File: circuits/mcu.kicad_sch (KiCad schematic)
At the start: 36 parts, among them J1 USB_MINI_B, J2 USB_MINI_B, J7 C192300, Q5 Q_L8050QLT1G, Q6 Q_L8550HQLT1G, SW1 SW_PUSH, SW2 SW_PUSH, SW3 SW_PUSH, U10 CP2102N-Axx-xQFN28, U9 ESP32-S3-WROOM-1

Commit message: Resolve USB connector source match
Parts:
- J1, J2: LCSC C46391 -> C5120592; Part Number 920-462A2021S10101 -> 65100516121
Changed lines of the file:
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@@
       (effects (font (size 1.27 1.27)) hide)
     )
-    (property "Part Number" "920-462A2021S10101" (at 129.8956 185.1914 0)
+    (property "Part Number" "65100516121" (at 129.8956 185.1914 0)
       (effects (font (size 1.27 1.27)) hide)
     )
@@
       (effects (font (size 1.27 1.27)) hide)
     )
-    (property "LCSC" "C46391" (at 132.4356 208.0514 0)
+    (property "LCSC" "C5120592" (at 132.4356 208.0514 0)
       (effects (font (size 1.27 1.27)) hide)
     )
@@
       (effects (font (size 1.27 1.27)) hide)
     )
-    (property "Part Number" "920-462A2021S10101" (at 131.9276 144.5514 0)
+    (property "Part Number" "65100516121" (at 131.9276 144.5514 0)
       (effects (font (size 1.27 1.27)) hide)
     )
@@
       (effects (font (size 1.27 1.27)) hide)
     )
-    (property "LCSC" "C46391" (at 134.4676 167.4114 0)
-      (effects (font (size 1.27 1.27)) hide)
-    )
+    (property "LCSC" "C5120592" (at 134.4676 167.4114 0)
+      (effects (font (size 1.27 1.27)) hide)
+    )

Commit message: Checkpoint laser controller fab parity package
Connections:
- net CP2102_VBUS: now reaches C45.1, R55.1, R56.2, U10.8 (VBUS)
- net USB_NATIVE_CONN_VBUS: now reaches D13.2 (A), J2.1 (VBUS)
- net CP2102_RST: now reaches R57.2, U10.9 (~{RST})
- net CP2102_SUSPEND_N: now reaches R58.1, U10.11 (~{SUSPEND})
- net AUTO_EN_BASE: now reaches Q5.1 (B), R50.2
- net USB_UART_CONN_VBUS: now reaches D10.2 (A), J1.1 (VBUS)
- net AUTO_BOOT_BASE: now reaches Q6.1 (B), R51.2

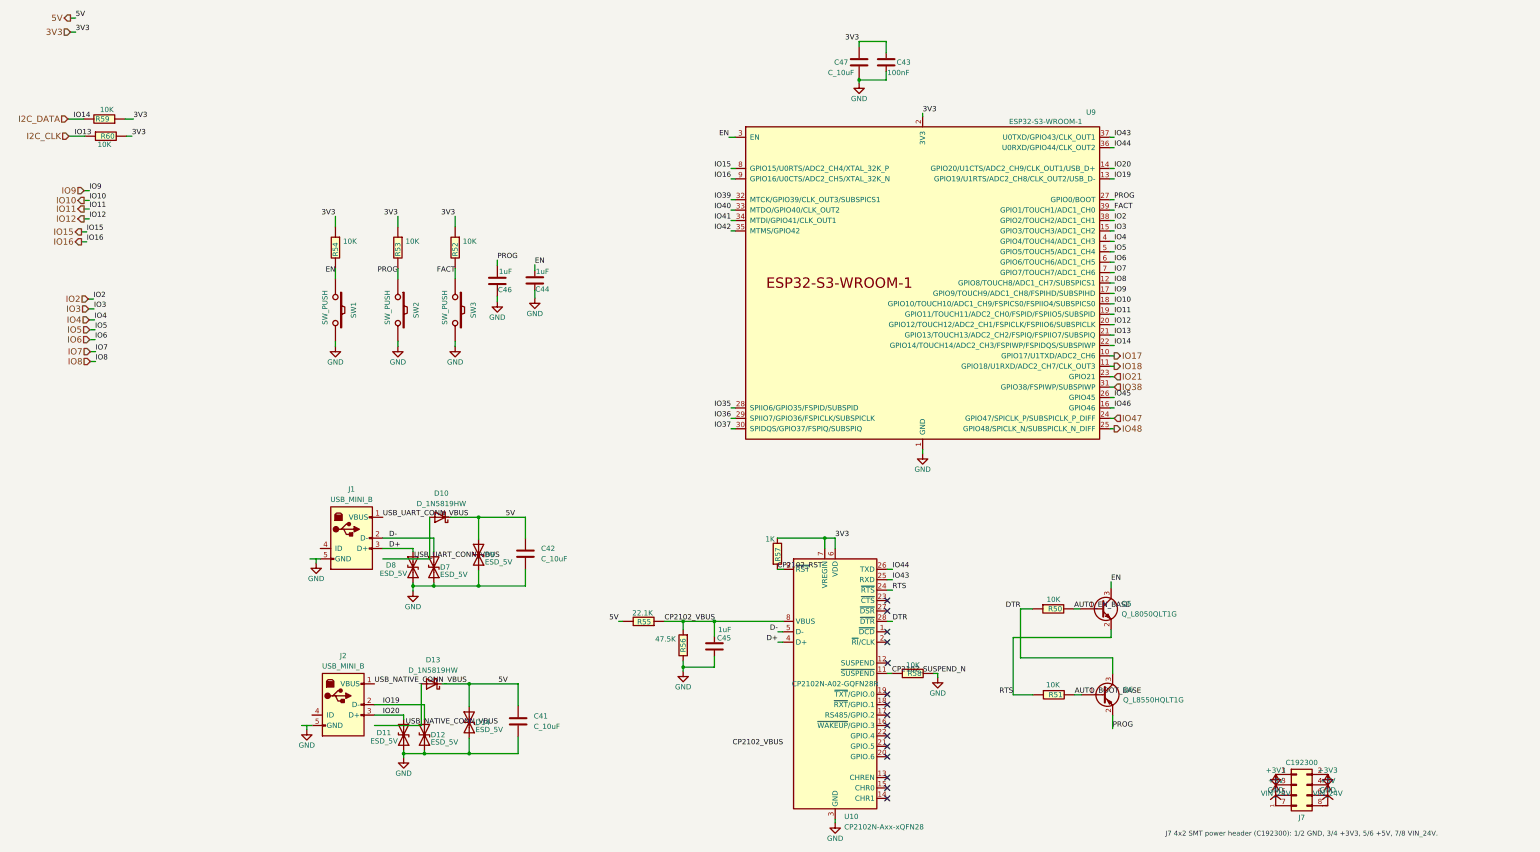
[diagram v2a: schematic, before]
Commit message: Checkpoint schematic ERC errors
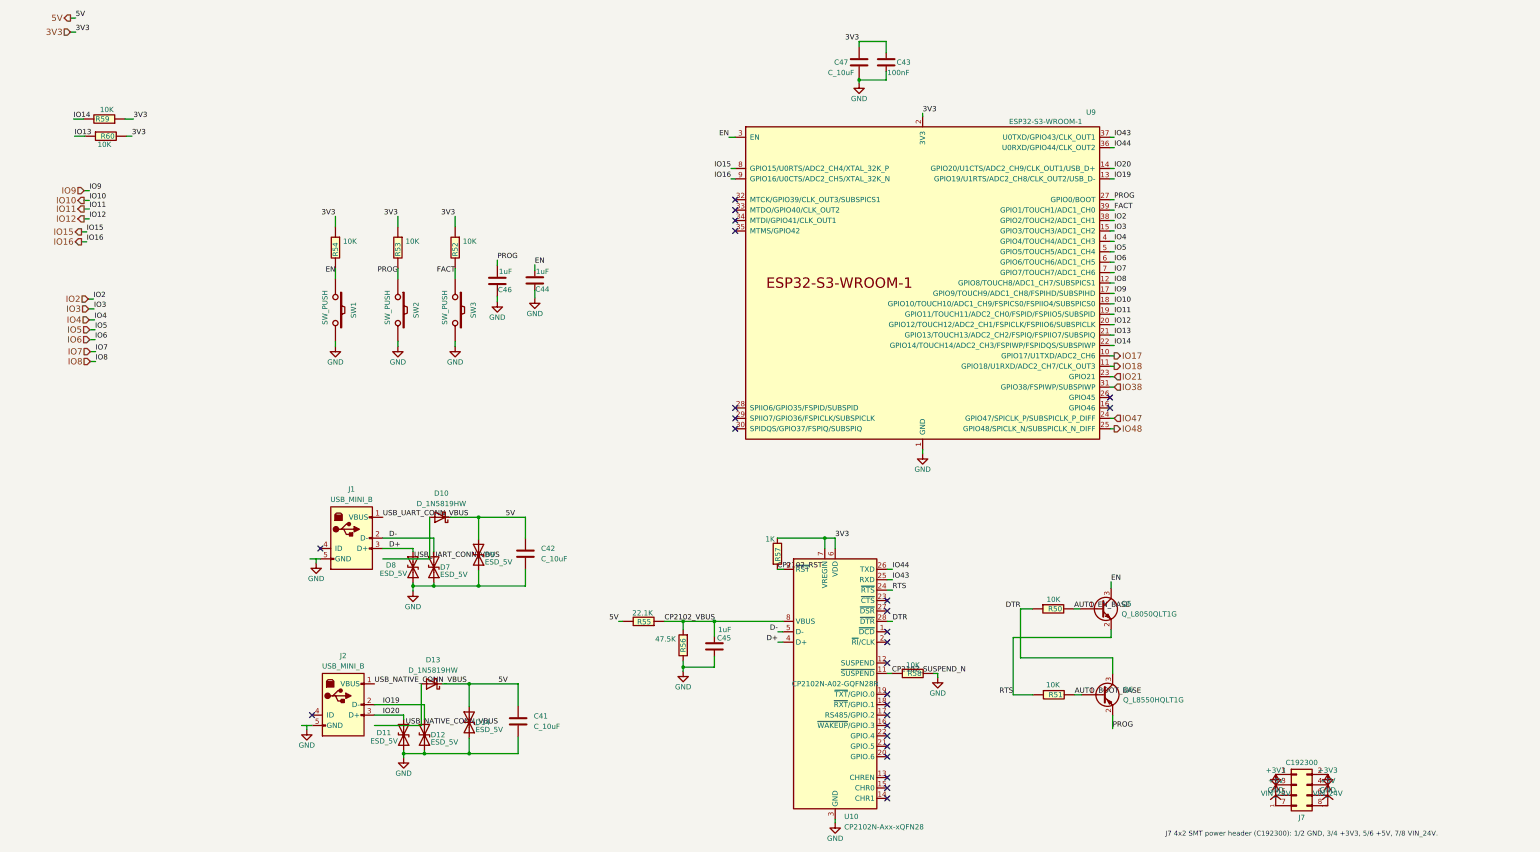
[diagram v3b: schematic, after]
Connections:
- net I2C_CLK renamed IO13
- net I2C_DATA renamed IO14
- net IO35: no longer names the net of U9.28 (SPIIO6/GPIO35/FSPID/SUBSPID)
- net IO36: no longer names the net of U9.29 (SPIIO7/GPIO36/FSPICLK/SUBSPICLK)
- net IO37: no longer names the net of U9.30 (SPIDQS/GPIO37/FSPIQ/SUBSPIQ)
- net IO39: no longer names the net of U9.32 (MTCK/GPIO39/CLK_OUT3/SUBSPICS1)
- net IO40: no longer names the net of U9.33 (MTDO/GPIO40/CLK_OUT2)
- net IO41: no longer names the net of U9.34 (MTDI/GPIO41/CLK_OUT1)
- net IO42: no longer names the net of U9.35 (MTMS/GPIO42)
- net IO45: no longer names the net of U9.26 (GPIO45)
- net IO46: no longer names the net of U9.16 (GPIO46)
- no-connect marks 15 -> 26
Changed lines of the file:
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@@
   (no_connect (at 265.1506 211.8614))
   (no_connect (at 265.1506 209.3214))
-  (no_connect (at 265.2776 189.0014))
+  (no_connect (at 265.1506 189.0014))
   (no_connect (at 265.1506 183.9214))
   (no_connect (at 265.1506 204.2414))
   (no_connect (at 265.1506 199.1614))
   (no_connect (at 265.1506 176.3014))
+  (no_connect (at 126.8476 161.0614))
+  (no_connect (at 124.8156 201.7014))
+  (no_connect (at 228.0666 75.9714))
+  (no_connect (at 228.0666 78.5114))
+  (no_connect (at 228.0666 81.0514))
+  (no_connect (at 228.0666 83.5914))
+  (no_connect (at 228.0666 126.7714))
+  (no_connect (at 228.0666 129.3114))
+  (no_connect (at 228.0666 131.8514))
+  (no_connect (at 319.5066 124.2314))
+  (no_connect (at 319.5066 126.7714))
   (wire (pts (xy 142.0876 163.6014) (xy 153.5176 163.6014))
     (stroke (width 0) (type default))
@@
     (stroke (width 0) (type default))
   )
-  (wire (pts (xy 320.5226 124.2314) (xy 319.5066 124.2314))
-    (stroke (width 0) (type default))
-  )
   (wire (pts (xy 147.1676 211.0994) (xy 147.1676 212.1154))
     (stroke (width 0) (type default))
@@
     (stroke (width 0) (type default))
   )
-  (wire (pts (xy 227.0506 78.5114) (xy 228.0666 78.5114))
-    (stroke (width 0) (type default))
-  )
   (wire (pts (xy 147.1676 210.3374) (xy 147.1676 211.0994))
     (stroke (width 0) (type default))
@@
     (stroke (width 0) (type default))
   )
-  (wire (pts (xy 227.0506 81.0514) (xy 228.0666 81.0514))
-    (stroke (width 0) (type default))
-  )
   (wire (pts (xy 215.3666 178.8414) (xy 215.3666 180.8734))
     (stroke (width 0) (type default))
@@
     (stroke (width 0) (type default))
   )
-  (wire (pts (xy 227.0506 126.7714) (xy 228.0666 126.7714))
-    (stroke (width 0) (type default))
-  )
   (wire (pts (xy 320.5226 75.9714) (xy 319.5066 75.9714))
     (stroke (width 0) (type default))
@@
     (stroke (width 0) (type default))
   )
-  (wire (pts (xy 65.5066 60.4774) (xy 69.4436 60.4774))
+  (wire (pts (xy 66.9036 60.4774) (xy 69.4436 60.4774))
     (stroke (width 0) (type default))
   )
@@
     (stroke (width 0) (type default))
   )
-  (wire (pts (xy 227.0506 75.9714) (xy 228.0666 75.9714))
-    (stroke (width 0) (type default))
-  )
   (wire (pts (xy 147.1676 201.7014) (xy 140.0556 201.7014))
     (stroke (width 0) (type default))
@@
     (stroke (width 0) (type default))
   )
-  (wire (pts (xy 227.0506 83.5914) (xy 228.0666 83.5914))
-    (stroke (width 0) (type default))
-  )
-  (wire (pts (xy 227.0506 129.3114) (xy 228.0666 129.3114))
-    (stroke (width 0) (type default))
-  )
-  (wire (pts (xy 320.5226 126.7714) (xy 319.5066 126.7714))
-    (stroke (width 0) (type default))
-  )
   (wire (pts (xy 227.0506 70.8914) (xy 228.0666 70.8914))
     (stroke (width 0) (type default))
@@
     (stroke (width 0) (type default))
   )
-  (wire (pts (xy 65.2526 56.2864) (xy 69.0626 56.2864))
+  (wire (pts (xy 66.6496 56.2864) (xy 69.0626 56.2864))
     (stroke (width 0) (type default))
   )
@@
     (stroke (width 0) (type default))
   )
-  (wire (pts (xy 227.0506 131.8514) (xy 228.0666 131.8514))
-    (stroke (width 0) (type default))
-  )
   (wire (pts (xy 149.4536 170.2054) (xy 149.4536 171.4754))
     (stroke (width 0) (type default))
@@
     (effects (font (size 1.27 1.27)) (justify right bottom))
   )
-  (label "IO39" (at 227.0506 75.9714 180) (fields_autoplaced)
-    (effects (font (size 1.27 1.27)) (justify right bottom))
-  )
   (label "IO11" (at 320.5226 103.9114 0) (fields_autoplaced)
     (effects (font (size 1.27 1.27)) (justify left bottom))
@@
     (effects (font (size 1.27 1.27)) (justify right bottom))
   )
-  (label "IO41" (at 227.0506 81.0514 180) (fields_autoplaced)
-    (effects (font (size 1.27 1.27)) (justify right bottom))
-  )
   (label "IO43" (at 266.4206 168.6814 0) (fields_autoplaced)
     (effects (font (size 1.27 1.27)) (justify left bottom))
@@
     (effects (font (size 1.27 1.27)) (justify left bottom))
   )
-  (label "IO37" (at 227.0506 131.8514 180) (fields_autoplaced)
-    (effects (font (size 1.27 1.27)) (justify right bottom))
-  )
-  (label "IO42" (at 227.0506 83.5914 180) (fields_autoplaced)
-    (effects (font (size 1.27 1.27)) (justify right bottom))
-  )
   (label "PROG" (at 145.7706 94.0054 180) (fields_autoplaced)
     (effects (font (size 1.27 1.27)) (justify right bottom))
@@
     (effects (font (size 1.27 1.27)) (justify left bottom))
   )
-  (label "IO40" (at 227.0506 78.5114 180) (fields_autoplaced)
-    (effects (font (size 1.27 1.27)) (justify right bottom))
-  )
   (label "IO13" (at 66.9036 60.4774 0) (fields_autoplaced)
     (effects (font (size 1.27 1.27)) (justify left bottom))
   )
-  (label "IO45" (at 320.5226 124.2314 0) (fields_autoplaced)
-    (effects (font (size 1.27 1.27)) (justify left bottom))
-  )
   (label "IO10" (at 320.5226 101.3714 0) (fields_autoplaced)
     (effects (font (size 1.27 1.27)) (justify left bottom))
@@
     (effects (font (size 1.27 1.27)) (justify left bottom))
   )
-  (label "IO35" (at 227.0506 126.7714 180) (fields_autoplaced)
-    (effects (font (size 1.27 1.27)) (justify right bottom))
-  )
   (label "IO3" (at 71.628 102.616 0) (fields_autoplaced)
     (effects (font (size 1.27 1.27)) (justify left bottom))
@@
     (effects (font (size 1.27 1.27)) (justify left bottom))
   )
-  (label "IO46" (at 320.5226 126.7714 0) (fields_autoplaced)
-    (effects (font (size 1.27 1.27)) (justify left bottom))
-  )
   (label "D-" (at 143.6116 158.5214 0) (fields_autoplaced)
     (effects (font (size 1.27 1.27)) (justify left bottom))
   )
-  (label "IO36" (at 227.0506 129.3114 180) (fields_autoplaced)
-    (effects (font (size 1.27 1.27)) (justify right bottom))
-  )
   (label "IO5" (at 320.5226 88.6714 0) (fields_autoplaced)
     (effects (font (size 1.27 1.27)) (justify left bottom))
@@
   (label "CP2102_VBUS" (at 210.7946 178.8414 0)
     (effects (font (size 1.27 1.27)) (justify left bottom))
-  )
-  (label "CP2102_VBUS" (at 239.7506 209.3214 180)
-    (effects (font (size 1.27 1.27)) (justify right bottom))
   )
   (label "CP2102_RST" (at 238.3536 166.1414 0)
@@
     (effects (font (size 1.524 1.524)) (justify right))
   )
-  (hierarchical_label "I2C_DATA" (shape input) (at 65.2526 56.2864 180) (fields_autoplaced)
-    (effects (font (size 1.524 1.524)) (justify right))
-  )
   (hierarchical_label "IO6" (shape input) (at 70.612 110.109 180) (fields_autoplaced)
     (effects (font (size 1.524 1.524)) (justify right))
@@
     (effects (font (size 1.524 1.524)) (justify right))
   )
-  (hierarchical_label "I2C_CLK" (shape input) (at 65.5066 60.4774 180) (fields_autoplaced)
-    (effects (font (size 1.524 1.524)) (justify right))
-  )

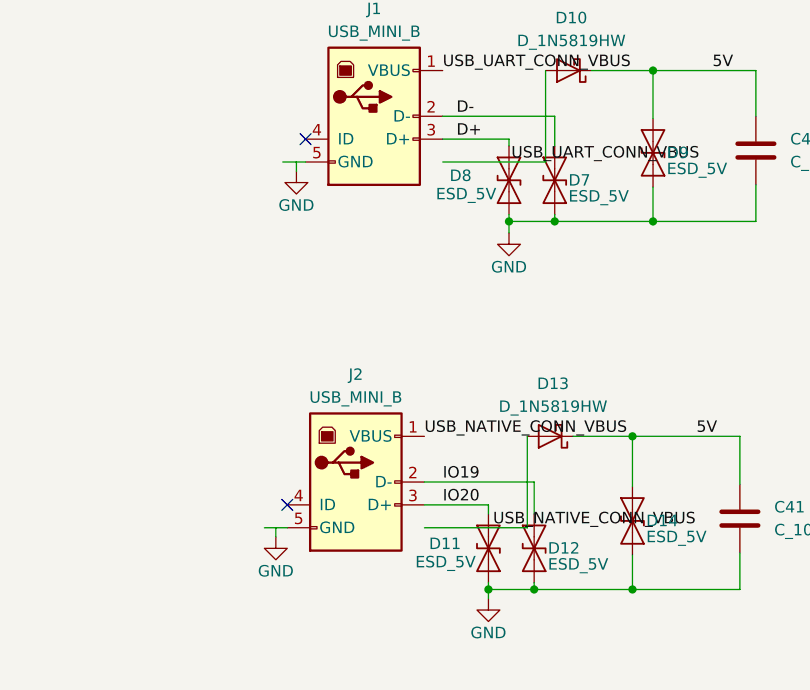
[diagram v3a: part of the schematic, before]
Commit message: Checkpoint schematic warning hygiene
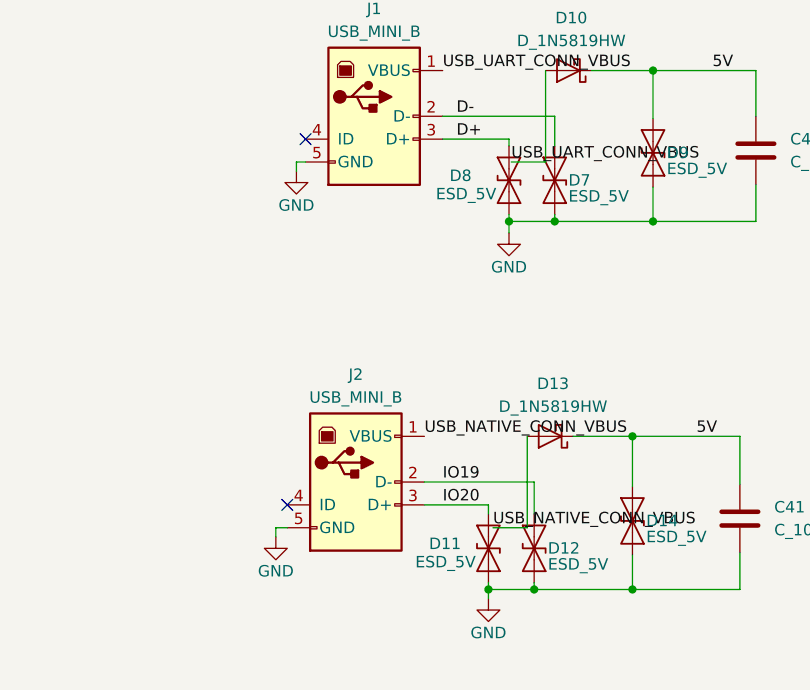
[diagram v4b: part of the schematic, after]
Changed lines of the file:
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@@
   (no_connect (at 319.5066 124.2314))
   (no_connect (at 319.5066 126.7714))
-  (wire (pts (xy 142.0876 163.6014) (xy 153.5176 163.6014))
+  (wire (pts (xy 149.7076 163.6014) (xy 153.5176 163.6014))
     (stroke (width 0) (type default))
   )
@@
     (stroke (width 0) (type default))
   )
-  (wire (pts (xy 124.3076 163.6014) (xy 125.8316 163.6014))
-    (stroke (width 0) (type default))
-  )
   (wire (pts (xy 69.215 80.645) (xy 70.485 80.645))
     (stroke (width 0) (type default))
@@
     (stroke (width 0) (type default))
   )
-  (wire (pts (xy 140.0556 204.2414) (xy 151.4856 204.2414))
+  (wire (pts (xy 147.6756 204.2414) (xy 151.4856 204.2414))
     (stroke (width 0) (type default))
   )
@@
     (stroke (width 0) (type default))
   )
-  (wire (pts (xy 122.2756 204.2414) (xy 123.5456 204.2414))
-    (stroke (width 0) (type default))
-  )

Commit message: Prepare laser controller JLCPCB connector assembly package
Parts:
- J1, J2: LCSC C5120592 -> C46391; Part Number 65100516121 -> 920-462A2021S10101
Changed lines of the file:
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@@
       (effects (font (size 1.27 1.27)) hide)
     )
-    (property "Part Number" "65100516121" (at 129.8956 185.1914 0)
+    (property "Part Number" "920-462A2021S10101" (at 129.8956 185.1914 0)
       (effects (font (size 1.27 1.27)) hide)
     )
@@
       (effects (font (size 1.27 1.27)) hide)
     )
-    (property "LCSC" "C5120592" (at 132.4356 208.0514 0)
+    (property "LCSC" "C46391" (at 132.4356 208.0514 0)
       (effects (font (size 1.27 1.27)) hide)
     )
@@
       (effects (font (size 1.27 1.27)) hide)
     )
-    (property "Part Number" "65100516121" (at 131.9276 144.5514 0)
+    (property "Part Number" "920-462A2021S10101" (at 131.9276 144.5514 0)
       (effects (font (size 1.27 1.27)) hide)
     )
@@
       (effects (font (size 1.27 1.27)) hide)
     )
-    (property "LCSC" "C5120592" (at 134.4676 167.4114 0)
-      (effects (font (size 1.27 1.27)) hide)
-    )
+    (property "LCSC" "C46391" (at 134.4676 167.4114 0)
+      (effects (font (size 1.27 1.27)) hide)
+    )

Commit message: Fix JLCPCB connector assembly package
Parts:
- J1, J2: LCSC C46391 -> C53207143; Part Number 920-462A2021S10101 -> MINI-USB-5P
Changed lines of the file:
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@@
       (effects (font (size 1.27 1.27)) hide)
     )
-    (property "Part Number" "920-462A2021S10101" (at 129.8956 185.1914 0)
+    (property "Part Number" "MINI-USB-5P" (at 129.8956 185.1914 0)
       (effects (font (size 1.27 1.27)) hide)
     )
@@
       (effects (font (size 1.27 1.27)) hide)
     )
-    (property "LCSC" "C46391" (at 132.4356 208.0514 0)
+    (property "LCSC" "C53207143" (at 132.4356 208.0514 0)
       (effects (font (size 1.27 1.27)) hide)
     )
@@
       (effects (font (size 1.27 1.27)) hide)
     )
-    (property "Part Number" "920-462A2021S10101" (at 131.9276 144.5514 0)
+    (property "Part Number" "MINI-USB-5P" (at 131.9276 144.5514 0)
       (effects (font (size 1.27 1.27)) hide)
     )
@@
       (effects (font (size 1.27 1.27)) hide)
     )
-    (property "LCSC" "C46391" (at 134.4676 167.4114 0)
-      (effects (font (size 1.27 1.27)) hide)
-    )
+    (property "LCSC" "C53207143" (at 134.4676 167.4114 0)
+      (effects (font (size 1.27 1.27)) hide)
+    )

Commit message: Fix laser controller JLCPCB connector assembly package
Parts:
- J1, J2: LCSC C53207143 -> C91144; Part Number MINI-USB-5P -> U-M-M5SS-W-2
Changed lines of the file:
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@@
       (effects (font (size 1.27 1.27)) hide)
     )
-    (property "Part Number" "MINI-USB-5P" (at 129.8956 185.1914 0)
+    (property "Part Number" "U-M-M5SS-W-2" (at 129.8956 185.1914 0)
       (effects (font (size 1.27 1.27)) hide)
     )
@@
       (effects (font (size 1.27 1.27)) hide)
     )
-    (property "LCSC" "C53207143" (at 132.4356 208.0514 0)
+    (property "LCSC" "C91144" (at 132.4356 208.0514 0)
       (effects (font (size 1.27 1.27)) hide)
     )
@@
       (effects (font (size 1.27 1.27)) hide)
     )
-    (property "Part Number" "MINI-USB-5P" (at 131.9276 144.5514 0)
+    (property "Part Number" "U-M-M5SS-W-2" (at 131.9276 144.5514 0)
       (effects (font (size 1.27 1.27)) hide)
     )
@@
       (effects (font (size 1.27 1.27)) hide)
     )
-    (property "LCSC" "C53207143" (at 134.4676 167.4114 0)
-      (effects (font (size 1.27 1.27)) hide)
-    )
+    (property "LCSC" "C91144" (at 134.4676 167.4114 0)
+      (effects (font (size 1.27 1.27)) hide)
+    )

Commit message: Fix JLCPCB connector placement package
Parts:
- J1, J2: LCSC C91144 -> C46391; Part Number U-M-M5SS-W-2 -> 920-462A2021S10101
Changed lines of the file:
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@@
       (effects (font (size 1.27 1.27)) hide)
     )
-    (property "Part Number" "U-M-M5SS-W-2" (at 129.8956 185.1914 0)
+    (property "Part Number" "920-462A2021S10101" (at 129.8956 185.1914 0)
       (effects (font (size 1.27 1.27)) hide)
     )
@@
       (effects (font (size 1.27 1.27)) hide)
     )
-    (property "LCSC" "C91144" (at 132.4356 208.0514 0)
+    (property "LCSC" "C46391" (at 132.4356 208.0514 0)
       (effects (font (size 1.27 1.27)) hide)
     )
@@
       (effects (font (size 1.27 1.27)) hide)
     )
-    (property "Part Number" "U-M-M5SS-W-2" (at 131.9276 144.5514 0)
+    (property "Part Number" "920-462A2021S10101" (at 131.9276 144.5514 0)
       (effects (font (size 1.27 1.27)) hide)
     )
@@
       (effects (font (size 1.27 1.27)) hide)
     )
-    (property "LCSC" "C91144" (at 134.4676 167.4114 0)
-      (effects (font (size 1.27 1.27)) hide)
-    )
+    (property "LCSC" "C46391" (at 134.4676 167.4114 0)
+      (effects (font (size 1.27 1.27)) hide)
+    )
